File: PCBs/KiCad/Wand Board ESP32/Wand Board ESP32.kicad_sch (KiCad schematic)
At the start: 27 parts, among them J10 ENC BTN, J11 ENCODER, J12 POW_IN, J13 BRL SENSE, J14 BAR, J15 DISP, J16 BODY LEDS, J17 VIBR, J19 BRL LEDS, J3 TIP LED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

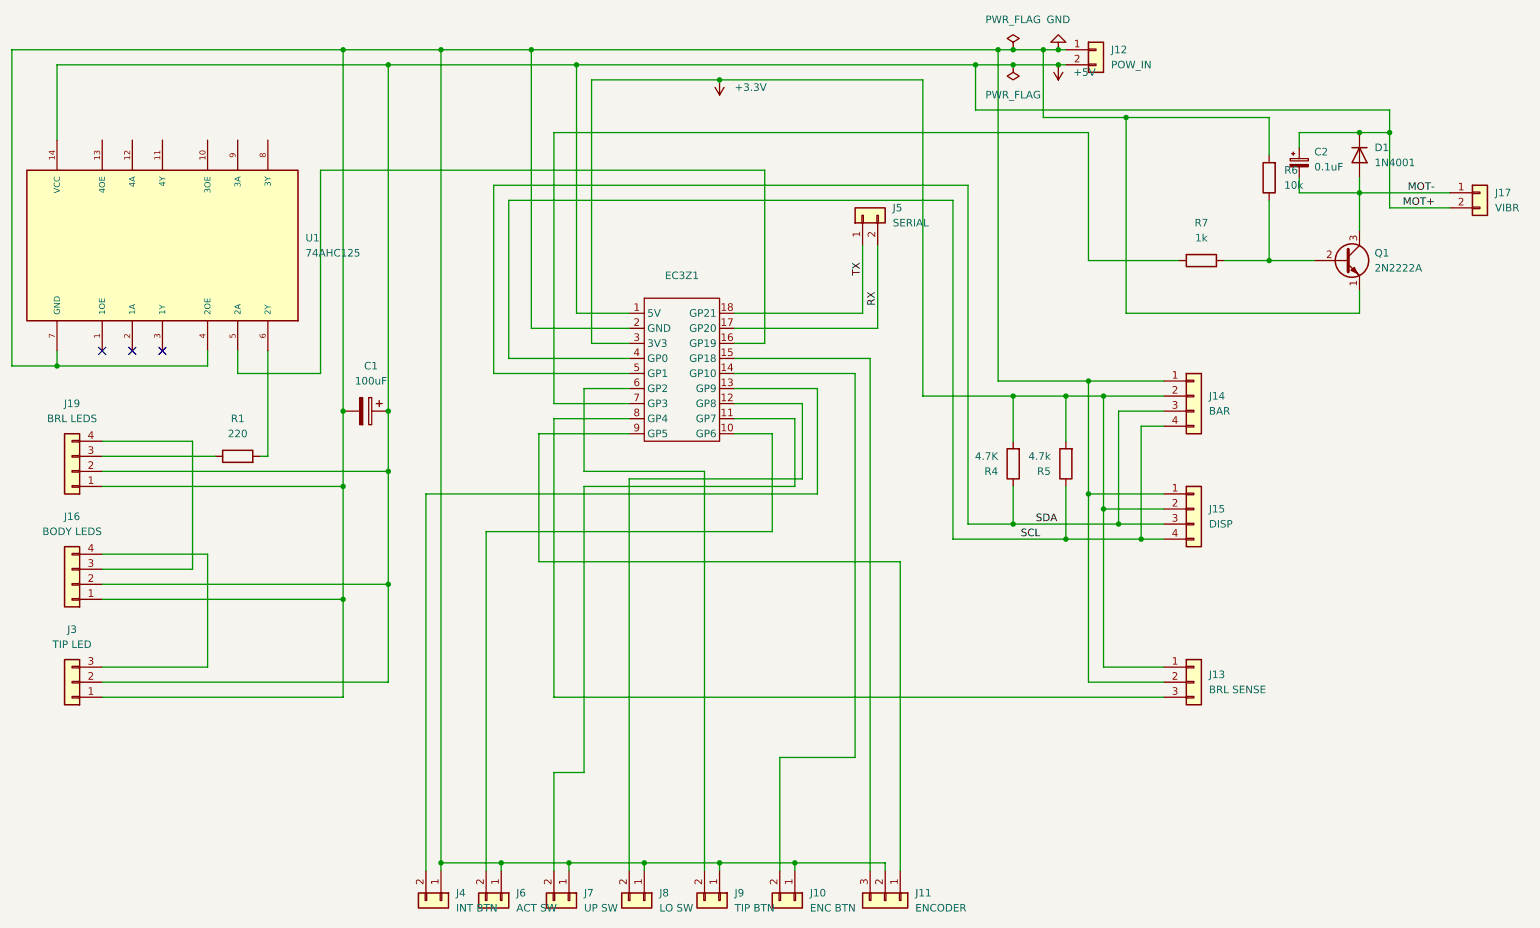
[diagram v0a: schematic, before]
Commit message: Tweaks to jigs, coloured schematics, readme notes
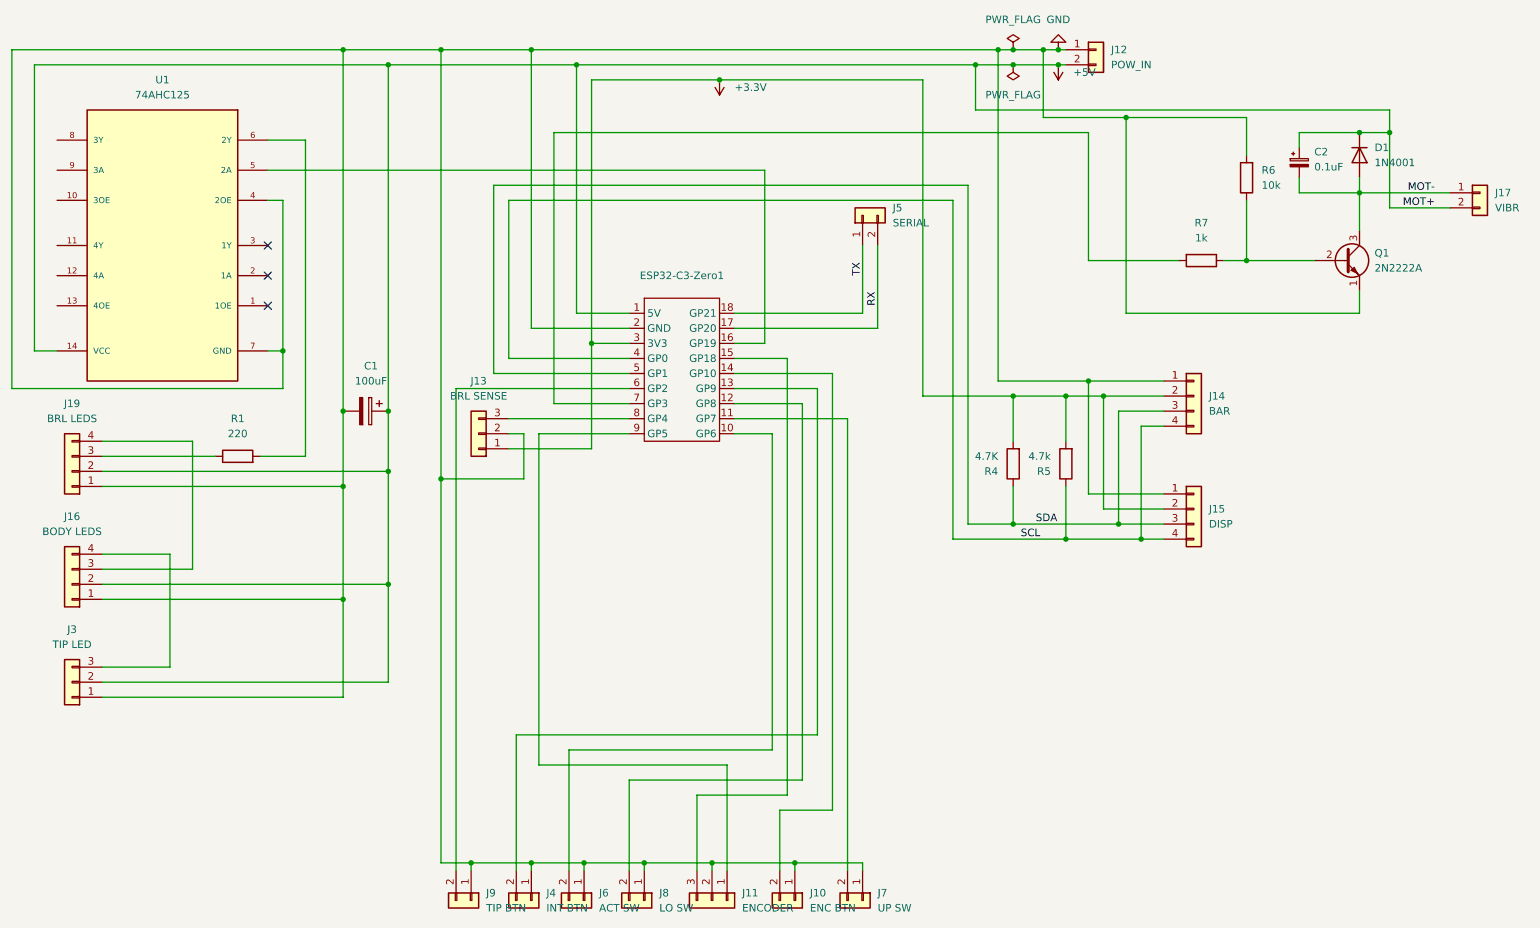
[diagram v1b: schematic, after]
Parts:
- renumbered EC3Z1 to ESP32-C3-Zero1
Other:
- moved on the sheet: J11, J13, J4, J6, J7, J9, R6, U1
